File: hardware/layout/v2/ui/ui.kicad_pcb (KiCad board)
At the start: 4 copper layers, 31.5 x 40.5 mm, 23 parts, among them J1 Controller cable, J2 OLED, SW1 PRG/RST, SW2 FUNC, U1 LM66100, U2 XIAO ESP32C6, U3 74AHCT1G125

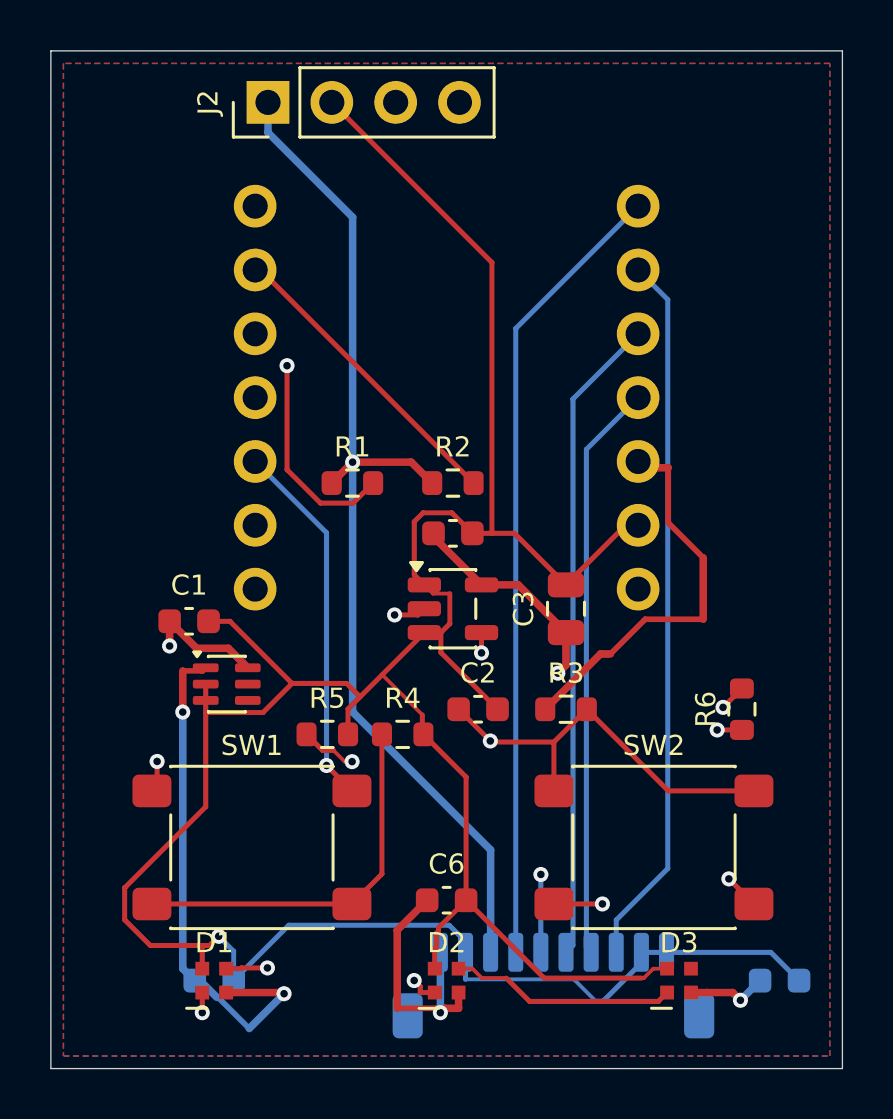
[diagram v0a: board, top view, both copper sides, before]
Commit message: Updated V2 UI board placement for centered front legend alignment; added legend color model generation to CI workflow
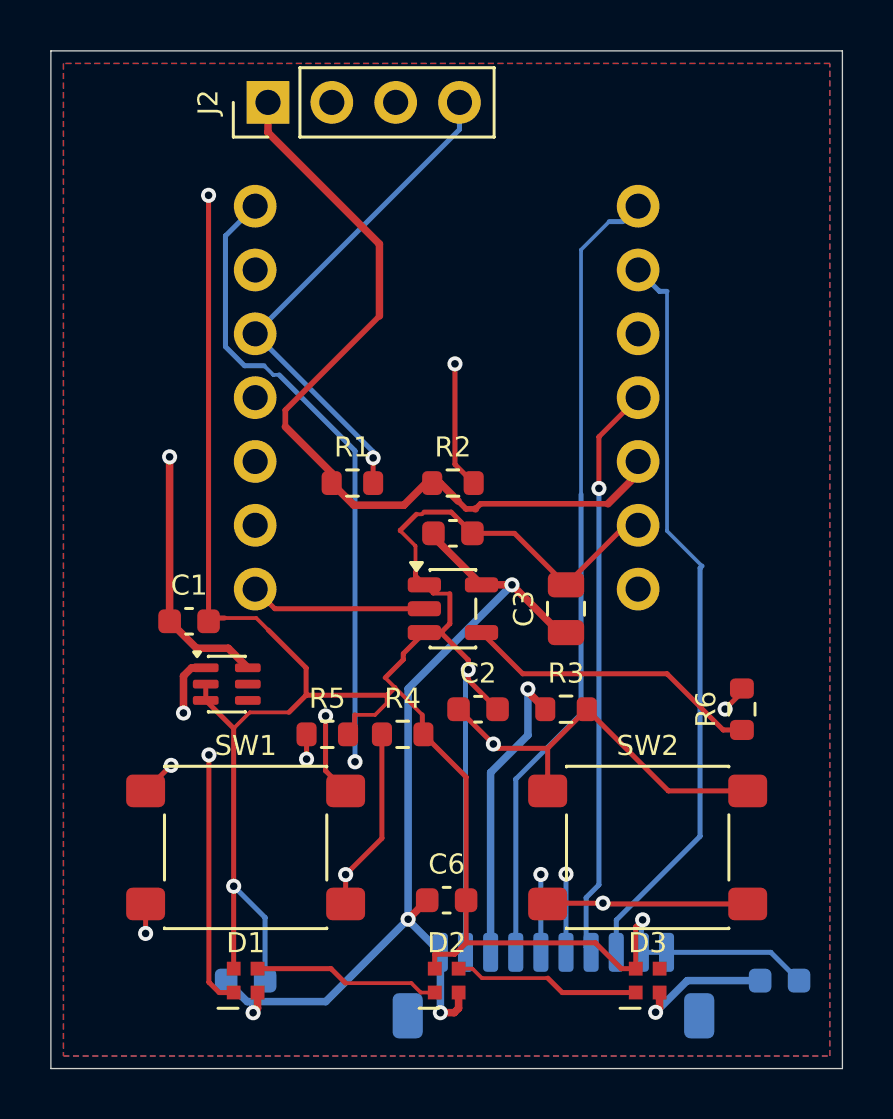
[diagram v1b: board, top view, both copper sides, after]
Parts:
- moved C5 1.25 mm to (7.75, -3.50)
- moved D1 1.25 mm to (7.75, -3.50)
- moved D3 1.25 mm to (23.8, -3.50)
- moved SW1 0.25 mm to (7.75, -8.80)
- moved SW2 0.25 mm to (23.8, -8.80)
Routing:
- net +5V_XIAO: track 24.4 -> 38.6 mm
- net +3V3: track 69.2 -> 56.8 mm
- net KNX_RXD: track 45.3 -> 37.7 mm, vias 1 -> 2
- net +5V: track 77.3 -> 71.2 mm, vias 5 -> 6
- net I2C_SCL: track 21.2 -> 26.8 mm, vias 0 -> 1
- net NCN_SAVEB: track 25.8 -> 30.5 mm, vias 0 -> 1
- net GND: track 125.8 -> 121.9 mm, vias 1 -> 4
- net N$4: track 33.0 -> 36.0 mm
- net I2C_SDA: track 22.8 -> 20.5 mm
- net N$1: track 15.2 -> 17.5 mm, vias 0 -> 2
- net LED_CHAIN2: track 8.99 -> 7.44 mm
- net LED_CHAIN1: track 8.86 -> 7.44 mm, vias 2 -> 0
- net DALI_RX: track 28.5 -> 29.8 mm
- net N$3: track 12.4 -> 12.0 mm, vias 2 -> 0
- net N$2: track 23.4 -> 23.1 mm, vias 3 -> 2
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
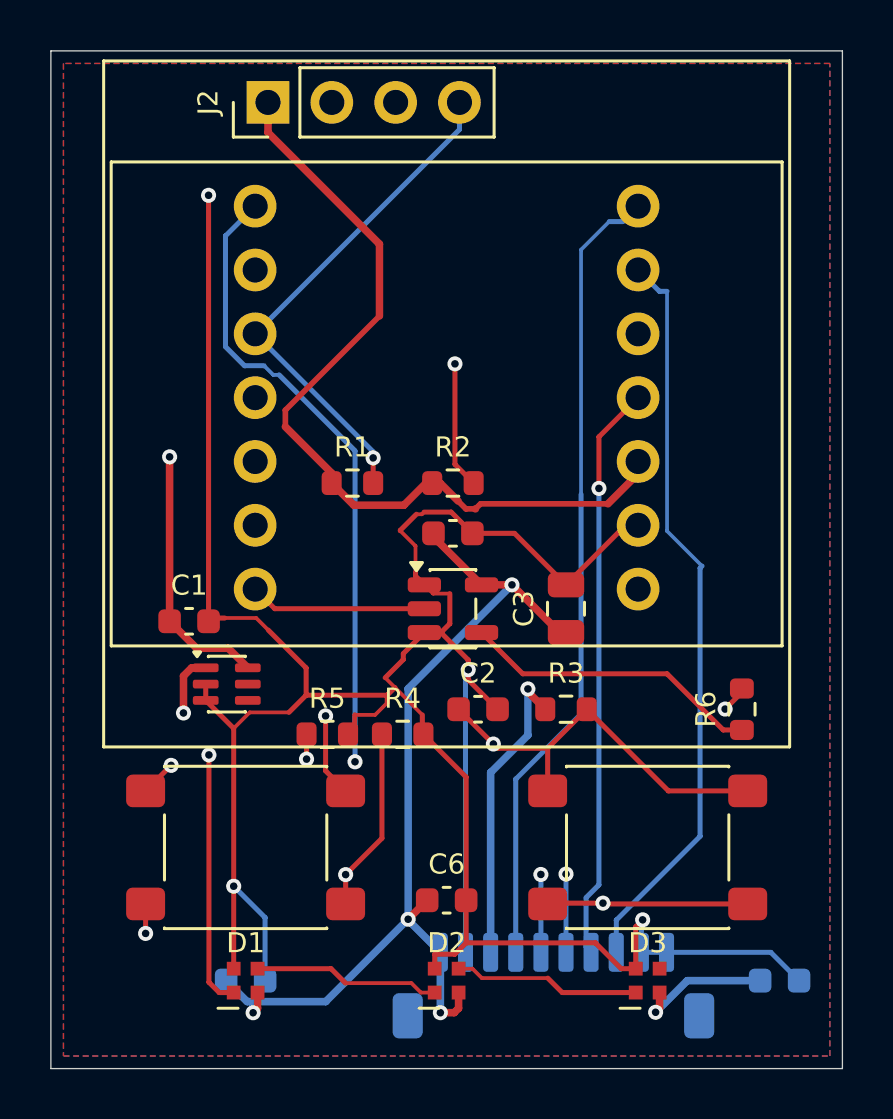
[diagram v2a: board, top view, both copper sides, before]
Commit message: V3 consolidated to two boards (main + ui); updated firmware pin map, button ADC, and OLED connector; removed separate knx/dali boards from CI matrix
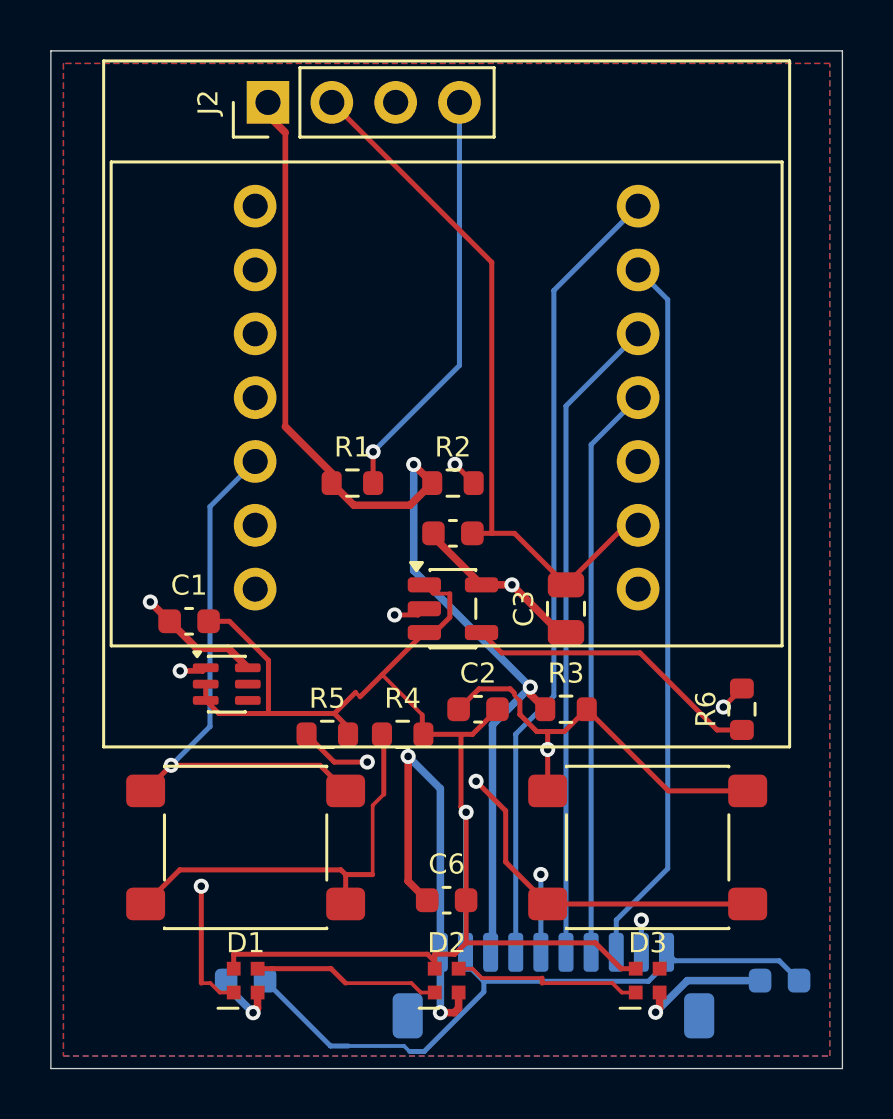
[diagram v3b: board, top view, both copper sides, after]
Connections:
- J1 pad 9: GND -> DALI_SUPPLY_OFF
- U2 pad 2: (no net) -> DALI_SUPPLY_OFF
- U2 pad 4: LED_DALI -> (no net)
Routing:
- net DALI_SUPPLY_OFF: track 0.00 -> 40.4 mm, vias 0 -> 1
- net +5V_XIAO: track 38.6 -> 25.6 mm
- net KNX_RXD: track 37.7 -> 49.2 mm, vias 2 -> 1
- net BTN_LADDER: track 46.0 -> 56.7 mm, vias 3 -> 2
- net GND: track 121.9 -> 128.7 mm, vias 4 -> 1
- net N$4: track 36.0 -> 30.1 mm
- net I2C_SCL: track 26.8 -> 21.2 mm
- net NCN_SAVEB: track 30.5 -> 25.8 mm, vias 1 -> 0
- net I2C_SDA: track 20.5 -> 23.2 mm
- net +3V3: track 56.8 -> 54.6 mm, vias 1 -> 2
- net N$2: track 23.1 -> 21.5 mm
- net +5V: track 71.2 -> 69.8 mm
- net DALI_RX: track 29.8 -> 28.5 mm
- net N$1: track 17.5 -> 16.6 mm, vias 2 -> 0
- net LED_DATA: track 7.06 -> 7.26 mm, vias 0 -> 1
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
